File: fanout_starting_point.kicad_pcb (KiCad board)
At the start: 10 copper layers, 200 x 125 mm, 8 parts, among them IC1 ADC12DL500ACF_Aligned, U1 MT53D512M16D1DS_Aligned, U2 FT601Q_Aligned, U3 Ti90G529_Functions

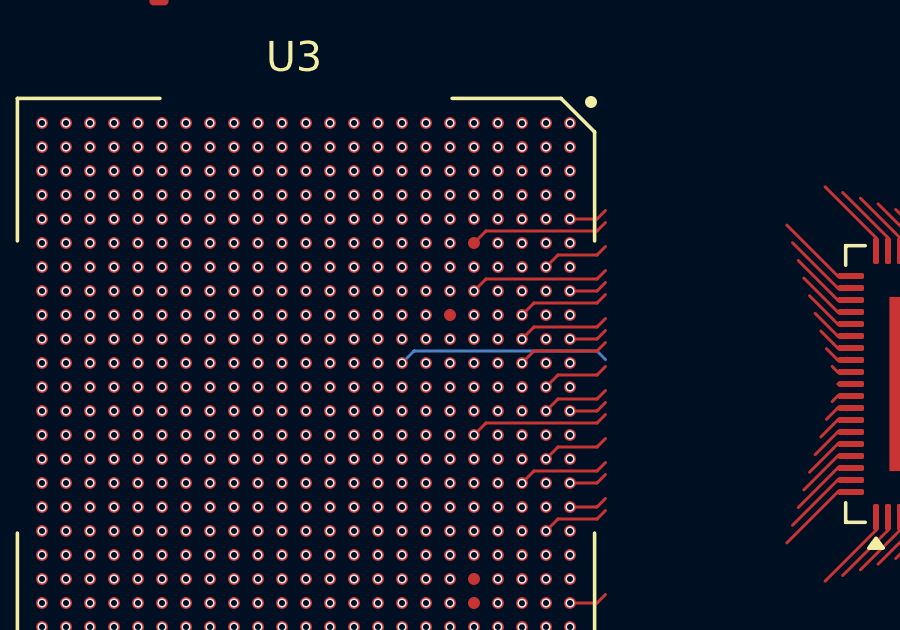
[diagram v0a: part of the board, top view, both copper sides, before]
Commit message: Remove weird segments near stubs that caused some drc errors
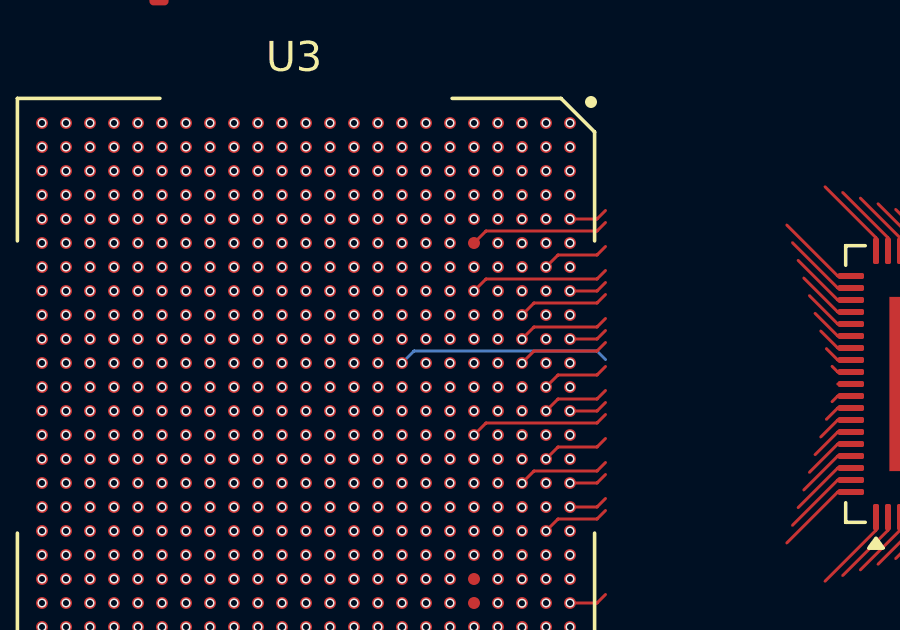
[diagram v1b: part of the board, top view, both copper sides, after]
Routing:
- net Net-(U2A-DATA_0): vias 0 -> 1
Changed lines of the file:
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@@
+		(net 302)
+	)
+	(via
+		(at 200.2 100.6)
+		(size 0.3)
+		(drill 0.2)
+		(layers "F.Cu" "B.Cu")
 		(net 302)
 	)
